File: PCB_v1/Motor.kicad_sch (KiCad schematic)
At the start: 20 parts, among them M1 Stepper_Motor_bipolar, U4 DRV8834PWP

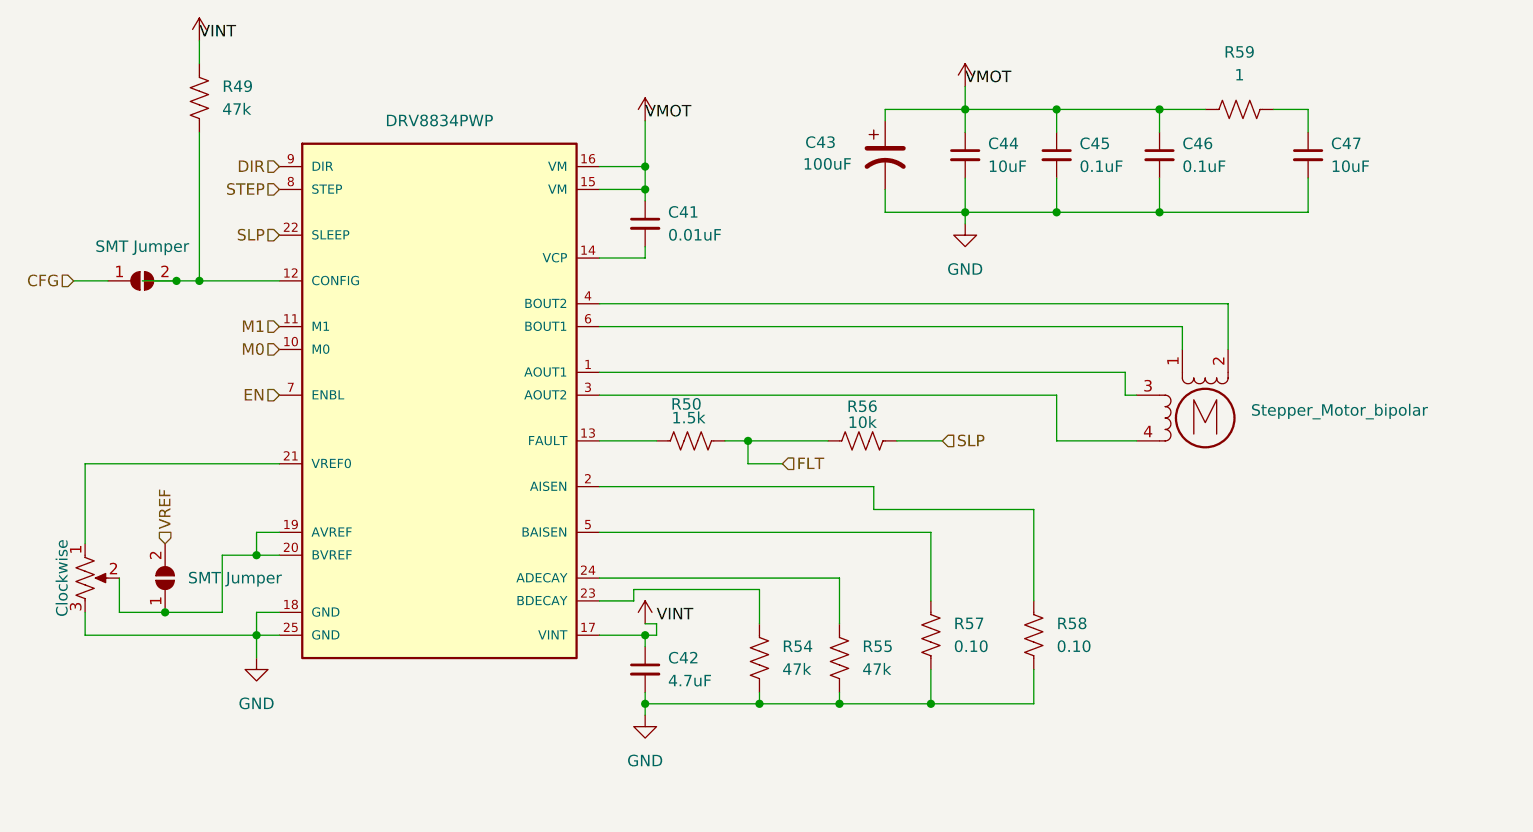
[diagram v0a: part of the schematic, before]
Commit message: adding the parts library
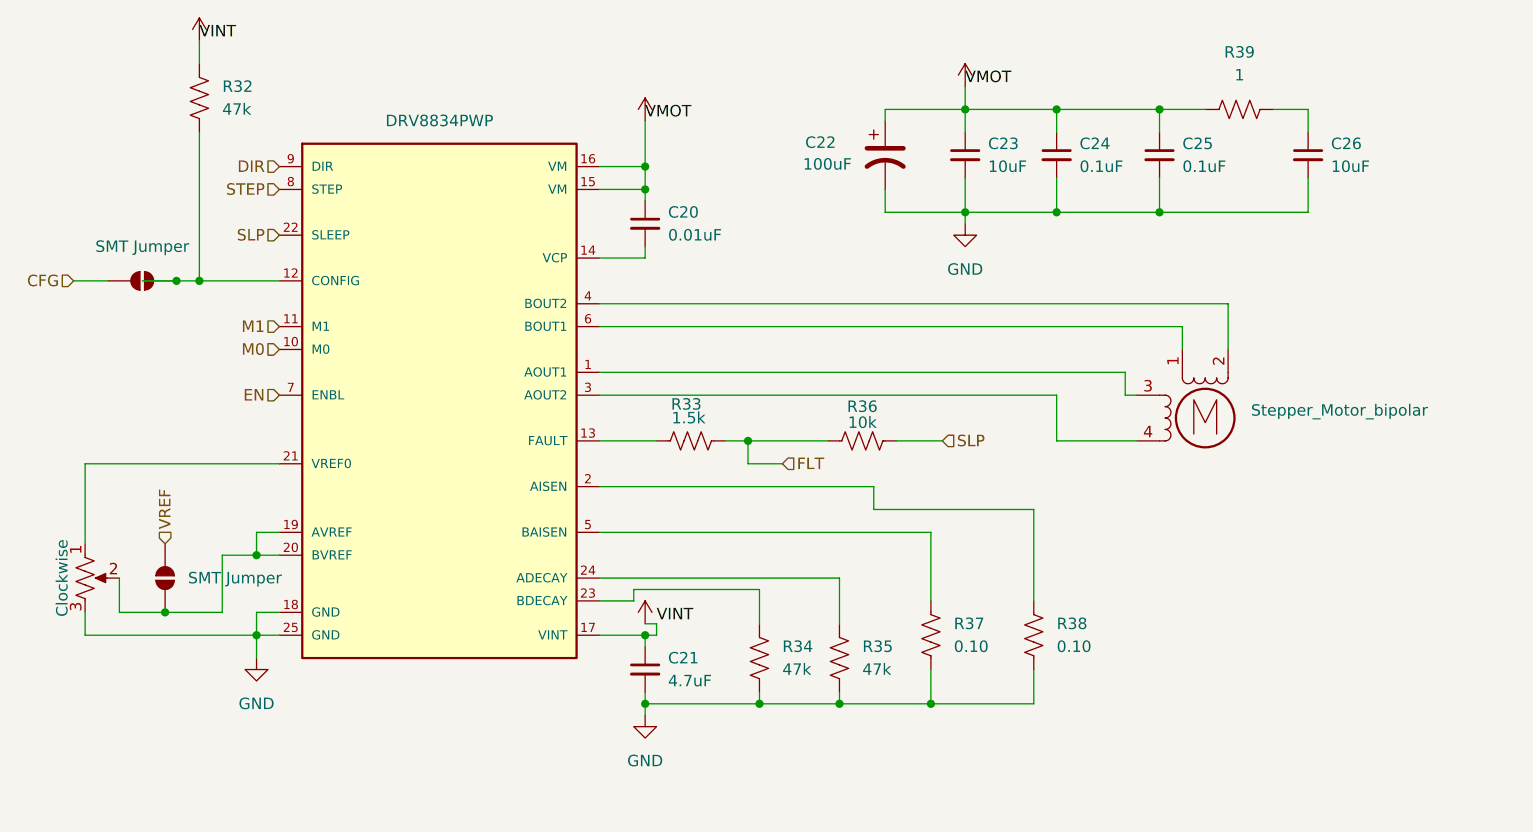
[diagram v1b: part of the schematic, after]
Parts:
- C20: renamed from C41; footprint (none) -> Capacitor_SMD:C_0805_2012Metric
- C21: renamed from C42; footprint (none) -> Capacitor_SMD:C_0805_2012Metric
- C23: renamed from C44; footprint (none) -> Capacitor_SMD:C_0805_2012Metric
- C24: renamed from C45; footprint (none) -> Capacitor_SMD:C_0805_2012Metric
- C25: renamed from C46; footprint (none) -> Capacitor_SMD:C_0805_2012Metric
- C26: renamed from C47; footprint (none) -> Capacitor_SMD:C_0805_2012Metric
- R32: renamed from R49; footprint (none) -> Resistor_SMD:R_0805_2012Metric
- R33: renamed from R50; footprint (none) -> Resistor_SMD:R_0805_2012Metric
- R34: renamed from R54; footprint (none) -> Resistor_SMD:R_0805_2012Metric
- R35: renamed from R55; footprint (none) -> Resistor_SMD:R_0805_2012Metric
- R36: renamed from R56; footprint (none) -> Resistor_SMD:R_0805_2012Metric
- R37: renamed from R57; footprint (none) -> Resistor_SMD:R_0805_2012Metric
- R38: renamed from R58; footprint (none) -> Resistor_SMD:R_0805_2012Metric
- R39: renamed from R59; footprint (none) -> Resistor_SMD:R_0805_2012Metric
- renumbered C43 to C22, JP4 to JP1, JP5 to JP2, U4 to U3

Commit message: Add files via upload
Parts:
- removed JP1, JP2: SMT Jumper, symbol Jumper:SolderJumper_2_Open
- removed M1: Stepper_Motor_bipolar, symbol Motor:Stepper_Motor_bipolar
- removed R36: 10k, Resistor_SMD:R_0805_2012Metric, symbol Device:R_US
- R33: value 1.5k -> 11.5k
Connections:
- net FLT is gone; now on net SLP: R33.2
- net VREF: now also RV1.2, U3.19 (AVREF), U3.20 (BVREF)
- net B1: now reaches U3.6 (BOUT1)
- net B2: now reaches U3.4 (BOUT2)
- net A1: now reaches U3.1 (AOUT1)
- net A2: now reaches U3.3 (AOUT2)
- net EN: no longer names the net of U3.7 (ENBL)
- net VINT renamed 3V3
- net VMOT renamed 5V
- no-connect marks 0 -> 1
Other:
- moved on the sheet: R32

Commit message: Add files via upload
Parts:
- added J6: B4B-XH-A, CONN_B4B-XH-A_JST, symbol 2025-02-27_00-30-21:B4B-XH-A
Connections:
- net A1: no longer names the net of U3.1 (AOUT1)
- net A1: now also J6.3 (A1)
- net A2: no longer names the net of U3.3 (AOUT2)
- net A2: now also J6.4 (A2)
- net B1: no longer names the net of U3.6 (BOUT1)
- net B1: now also J6.2 (B1)
- net B2: no longer names the net of U3.4 (BOUT2)
- net B2: now also J6.1 (B2)
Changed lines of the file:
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@@
+	(wire
+		(pts
+			(xy 109.22 69.85) (xy 99.06 69.85)
+		)
+		(stroke
+			(width 0)
+			(type default)
+		)
+	)
 	(wire
 		(pts
@@
 	(wire
 		(pts
+			(xy 96.52 69.85) (xy 96.52 67.31)
+		)
+		(stroke
+			(width 0)
+			(type default)
+		)
+	)
+	(wire
+		(pts
 			(xy 114.3 106.68) (xy 101.6 106.68)
 		)
@@
 	(wire
 		(pts
+			(xy 99.06 72.39) (xy 96.52 72.39)
+		)
+		(stroke
+			(width 0)
+			(type default)
+		)
+	)
+	(wire
+		(pts
 			(xy 158.75 40.64) (xy 163.83 40.64)
 		)
@@
 	(wire
 		(pts
+			(xy 99.06 69.85) (xy 99.06 72.39)
+		)
+		(stroke
+			(width 0)
+			(type default)
+		)
+	)
+	(wire
+		(pts
+			(xy 96.52 64.77) (xy 109.22 64.77)
+		)
+		(stroke
+			(width 0)
+			(type default)
+		)
+	)
+	(wire
+		(pts
+			(xy 96.52 62.23) (xy 109.22 62.23)
+		)
+		(stroke
+			(width 0)
+			(type default)
+		)
+	)
+	(wire
+		(pts
 			(xy 175.26 43.18) (xy 175.26 40.64)
 		)
@@
 		(pts
 			(xy 58.42 87.63) (xy 58.42 90.17)
+		)
+		(stroke
+			(width 0)
+			(type default)
+		)
+	)
+	(wire
+		(pts
+			(xy 96.52 67.31) (xy 109.22 67.31)
 		)
 		(stroke
@@
 		)
 	)
-	(hierarchical_label "B1"
-		(shape input)
-		(at 96.52 64.77 0)
-		(effects
-			(font
-				(size 1.27 1.27)
-			)
-			(justify left)
-		)
-	)
 	(hierarchical_label "SLP"
 		(shape input)
@@
 		)
 	)
-	(hierarchical_label "A2"
-		(shape input)
-		(at 96.52 72.39 0)
-		(effects
-			(font
-				(size 1.27 1.27)
-			)
-			(justify left)
-		)
-	)
 	(hierarchical_label "M1"
 		(shape input)
@@
 		)
 	)
-	(hierarchical_label "A1"
-		(shape input)
-		(at 96.52 69.85 0)
-		(effects
-			(font
-				(size 1.27 1.27)
-			)
-			(justify left)
-		)
-	)
-	(hierarchical_label "B2"
-		(shape input)
-		(at 96.52 62.23 0)
-		(effects
-			(font
-				(size 1.27 1.27)
-			)
-			(justify left)
-		)
-	)
 	(hierarchical_label "DIR"
 		(shape input)
@@
 		)
 	)
+	(symbol
+		(lib_id "2025-02-27_00-30-21:B4B-XH-A")
+		(at 109.22 62.23 0)
+		(unit 1)
+		(exclude_from_sim no)
+		(in_bom yes)
+		(on_board yes)
+		(dnp no)
+		(fields_autoplaced yes)
+		(property "Reference" "J6"
+			(at 123.19 64.7699 0)
+			(effects
+				(font
+					(size 1.524 1.524)
+				)
+				(justify left)
+			)
+		)
+		(property "Value" "B4B-XH-A"
+			(at 123.19 67.3099 0)
+			(effects
+				(font
+					(size 1.524 1.524)
+				)
+				(justify left)
+			)
+		)
+		(property "Footprint" "CONN_B4B-XH-A_JST"
+			(at 109.22 62.23 0)
+			(effects
+				(font
+					(size 1.27 1.27)
+					(italic yes)
+				)
+				(hide yes)
+			)
+		)
+		(property "Datasheet" "B4B-XH-A"
+			(at 109.22 62.23 0)
+			(effects
+				(font
+					(size 1.27 1.27)
+					(italic yes)
+				)
+				(hide yes)
+			)
+		)
+		(property "Description" ""
+			(at 109.22 62.23 0)
+			(effects
+				(font
+					(size 1.27 1.27)
+				)
+				(hide yes)
+			)
+		)
+		(pin "1"
+		)
+		(pin "2"
+		)
+		(pin "3"
+		)
+		(pin "4"
+		)
+		(instances
+			(project ""
+				(path "/353cef6a-fb6e-40d9-89f8-eb54b7aa5118/2d8cfae4-f7d1-4a7d-b5cb-7588b4c1e8a5"
+					(reference "J6")
+					(unit 1)
+				)
+			)
+		)
+	)

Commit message: changed the MICs to JST headers
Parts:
- removed C20: 0.01uF, Capacitor_SMD:C_0805_2012Metric, symbol Device:C_Small
- removed C21: 4.7uF, Capacitor_SMD:C_0805_2012Metric, symbol Device:C_Small
- removed C22: 100uF, symbol Device:C_Polarized_US
- removed C23, C26: 10uF, Capacitor_SMD:C_0805_2012Metric, symbol Device:C_Small
- removed C24, C25: 0.1uF, Capacitor_SMD:C_0805_2012Metric, symbol Device:C_Small
- removed J6: B4B-XH-A, CONN_B4B-XH-A_JST, symbol 2025-02-27_00-30-21:B4B-XH-A
- removed R32, R34, R35: 47k, Resistor_SMD:R_0805_2012Metric, symbol Device:R_US
- removed R33: 11.5k, Resistor_SMD:R_0805_2012Metric, symbol Device:R_US
- removed R37, R38: 0.10, Resistor_SMD:R_0805_2012Metric, symbol Device:R_US
- removed R39: 1, Resistor_SMD:R_0805_2012Metric, symbol Device:R_US
- removed RV1: Clockwise, symbol Device:R_Potentiometer_US
- removed U3: DRV8834PWP, SOP65P640X120-25N, symbol DRV8834PWP:DRV8834PWP
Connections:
- no-connect marks 1 -> 0
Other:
- note removed: "Motor"

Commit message: PCB changes before changing Seth's clock
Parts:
- added C14, C6: 10uF, Capacitor_SMD:C_0805_2012Metric, symbol Device:C_Small
- added C3: 0.01uF, Capacitor_SMD:C_0805_2012Metric, symbol Device:C_Small
- added C4: 4.7uF, Capacitor_SMD:C_0805_2012Metric, symbol Device:C_Small
- added C5: 100uF, CAP_PAN_EEE_H13_PAN, symbol Device:C_Polarized_US
- added C7, C8: 0.1uF, Capacitor_SMD:C_0805_2012Metric, symbol Device:C_Small
- added J10: B4B-XH-A, B4B-XH-A:JST_B4B-XH-A, symbol GT_LIbrary:B4B-XH-A
- added R1, R3, R4: 47k, Resistor_SMD:R_0805_2012Metric, symbol Device:R_US
- added R2: 1.5k, Resistor_SMD:R_0805_2012Metric, symbol Device:R_US
- added R20: 1, Resistor_SMD:R_0805_2012Metric, symbol Device:R_US
- added R5: 10k, Resistor_SMD:R_0805_2012Metric, symbol Device:R_US
- added R6, R7: 0.10, Resistor_SMD:R_0805_2012Metric, symbol Device:R_US
- added RV1: Clockwise, symbol Device:R_Potentiometer_US
- added U6: DRV8834PWP, SOP65P640X120-25N, symbol DRV8834PWP:DRV8834PWP
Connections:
- new net: R1.2, U6.12 (CONFIG)
- new net: R3.1, U6.23 (BDECAY)
- new net: C14.1, R20.2
- new net: C3.2, U6.14 (VCP)
- new net: RV1.1, U6.21 (VREF0)
- new net: R4.1, U6.24 (ADECAY)
- new net: J10.3, U6.1 (AOUT1)
- new net: R2.1, U6.13 (FAULT)
- new net: R7.1, U6.2 (AISEN)
- new net: J10.4, U6.3 (AOUT2)
- new net: J10.1, U6.4 (BOUT2)
- new net: R6.1, U6.5 (BAISEN)
- new net: J10.2, U6.6 (BOUT1)
- new net DIR: U6.9 (DIR)
- new net EN: U6.7 (ENBL)
- new net FLT: R2.2, R5.1
- new net GND: C14.2, C4.2, C5.2, C6.2, C7.2, C8.2, R3.2, R4.2, R6.2, R7.2, RV1.3, U6.18 (GND), U6.25 (GND)
- new net M0: U6.10 (M0)
- new net M1: U6.11 (M1)
- new net SLP: R5.2, U6.22 (SLEEP)
- new net STEP: U6.8 (STEP)
- new net VINT: C4.1, R1.1, U6.17 (VINT)
- new net VMOT: C3.1, C5.1, C6.1, C7.1, C8.1, R20.1, U6.15 (VM), U6.16 (VM)
- new net VREF: RV1.2, U6.19 (AVREF), U6.20 (BVREF)
